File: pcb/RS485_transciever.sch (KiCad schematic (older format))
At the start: 27 parts, among them J1 RJ45_Shielded, J2 RJ45_Shielded, U103 ADM2687E

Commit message: fixing broken symbols
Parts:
- C111, C112, C113, C114, C115, C116, C117, C118: symbol antena:C_Small -> Device:C_Small
- R105: symbol antena:R_Small -> Device:R_Small
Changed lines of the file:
@@
 	4700 3550 4700 750
 $Comp
-L antena:C_Small C?
+L Device:C_Small C?
 U 1 1 5F862E69
 P 7300 2900
@@
 $EndComp
 $Comp
-L antena:C_Small C?
+L Device:C_Small C?
 U 1 1 5F862E6F
 P 7600 2900
@@
 $EndComp
 $Comp
-L antena:C_Small C?
+L Device:C_Small C?
 U 1 1 5F862E75
 P 7300 3200
@@
 $EndComp
 $Comp
-L antena:C_Small C?
+L Device:C_Small C?
 U 1 1 5F862E7B
 P 7600 3200
@@
 $EndComp
 $Comp
-L antena:C_Small C?
+L Device:C_Small C?
 U 1 1 5F862E81
 P 5150 2900
@@
 $EndComp
 $Comp
-L antena:C_Small C?
+L Device:C_Small C?
 U 1 1 5F862E87
 P 4850 2900
@@
 $EndComp
 $Comp
-L antena:C_Small C?
+L Device:C_Small C?
 U 1 1 5F862E8D
 P 5150 3200
@@
 $EndComp
 $Comp
-L antena:C_Small C?
+L Device:C_Small C?
 U 1 1 5F862E93
 P 4850 3200
@@
 Link Tx to Rx (Optional)
 $Comp
-L antena:R_Small R?
+L Device:R_Small R?
 U 1 1 5F862F44
 P 10150 5700

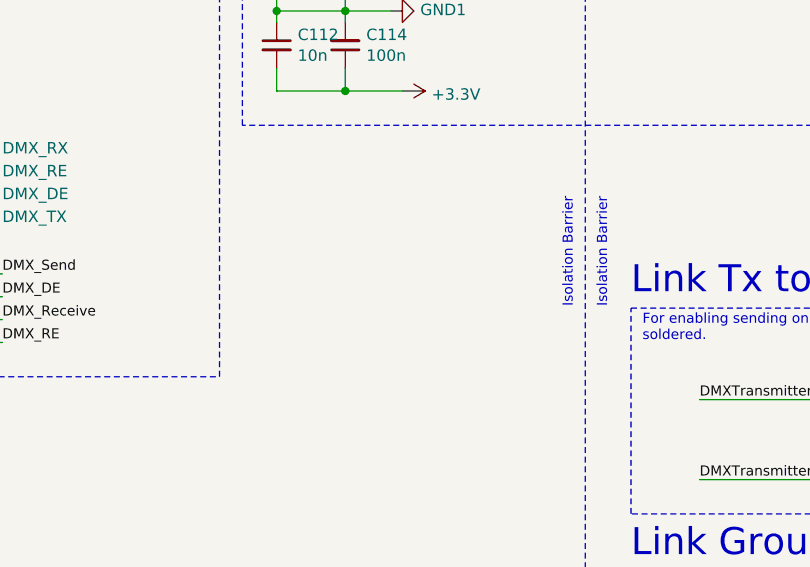
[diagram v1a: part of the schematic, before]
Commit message: Adding protection diodes
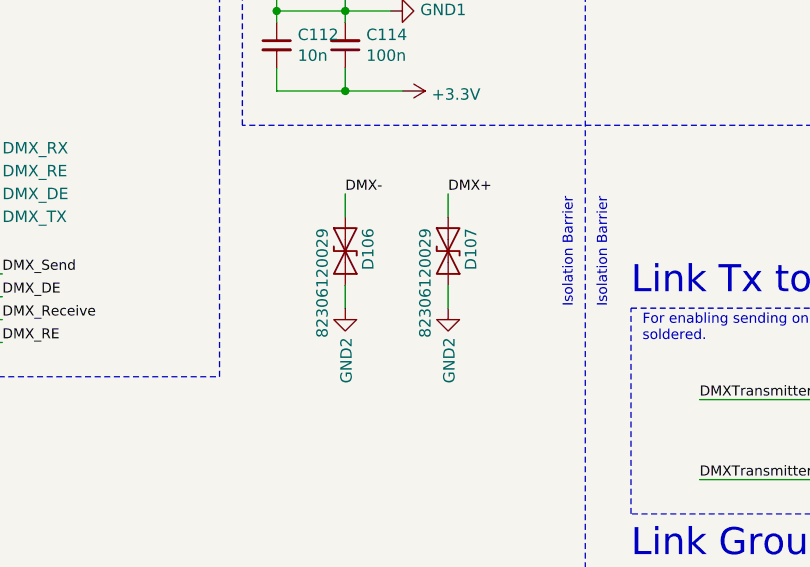
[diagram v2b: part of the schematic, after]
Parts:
- added D106, D107: 82306120029, Diode_SMD:D_0603_1608Metric, symbol Diode:ESD9B3.3ST5G
- JP105, JP106: footprint Jumper:SolderJumper-2_P1.3mm_Open_RoundedPad1.0x1.5mm -> Jumper:SolderJumper-2_P1.3mm_Bridged_RoundedPad1.0x1.5mm
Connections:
- wire segments 93 -> 97
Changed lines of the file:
@@
 F 0 "JP105" H 7650 4955 50  0000 C CNN
 F 1 "SolderJumper_2_Open" H 7650 4864 50  0000 C CNN
-F 2 "Jumper:SolderJumper-2_P1.3mm_Open_RoundedPad1.0x1.5mm" H 7650 4750 50  0001 C CNN
+F 2 "Jumper:SolderJumper-2_P1.3mm_Bridged_RoundedPad1.0x1.5mm" H 7650 4750 50  0001 C CNN
 F 3 "~" H 7650 4750 50  0001 C CNN
 	1    7650 4750
@@
 F 0 "JP106" H 7650 5305 50  0000 C CNN
 F 1 "SolderJumper_2_Open" H 7650 5214 50  0000 C CNN
-F 2 "Jumper:SolderJumper-2_P1.3mm_Open_RoundedPad1.0x1.5mm" H 7650 5100 50  0001 C CNN
+F 2 "Jumper:SolderJumper-2_P1.3mm_Bridged_RoundedPad1.0x1.5mm" H 7650 5100 50  0001 C CNN
 F 3 "~" H 7650 5100 50  0001 C CNN
 	1    7650 5100
@@
 Wire Wire Line
 	9600 1850 9600 1950
+Text Label 5150 3850 0    44   ~ 0
+DMX-
+Text Label 5600 3850 0    44   ~ 0
+DMX+
+$Comp
+L power:GND2 #PWR?
+U 1 1 6081C4D7
+P 5150 4350
+AR Path="/6081C4D7" Ref="#PWR?"  Part="1"
+AR Path="/5F845145/6081C4D7" Ref="#PWR07"  Part="1"
+F 0 "#PWR07" H 5150 4100 50  0001 C CNN
+F 1 "GND2" V 5155 4222 50  0000 R CNN
+F 2 "" H 5150 4350 50  0001 C CNN
+F 3 "" H 5150 4350 50  0001 C CNN
+	1    5150 4350
+	1    0    0    -1
+$EndComp
+$Comp
+L power:GND2 #PWR?
+U 1 1 6081CCE9
+P 5600 4350
+AR Path="/6081CCE9" Ref="#PWR?"  Part="1"
+AR Path="/5F845145/6081CCE9" Ref="#PWR08"  Part="1"
+F 0 "#PWR08" H 5600 4100 50  0001 C CNN
+F 1 "GND2" V 5605 4222 50  0000 R CNN
+F 2 "" H 5600 4350 50  0001 C CNN
+F 3 "" H 5600 4350 50  0001 C CNN
+	1    5600 4350
+	1    0    0    -1
+$EndComp
+Wire Wire Line
+	5150 3850 5150 3950
+Wire Wire Line
+	5600 3850 5600 3950
+Wire Wire Line
+	5150 4250 5150 4350
+Wire Wire Line
+	5600 4250 5600 4350
+$Comp
+L Diode:ESD9B3.3ST5G D?
+U 1 1 608502C5
+P 5150 4100
+AR Path="/608502C5" Ref="D?"  Part="1"
+AR Path="/5F845145/608502C5" Ref="D106"  Part="1"
+F 0 "D106" H 5050 4200 50  0000 L CNN
+F 1 "82306120029" H 5050 4000 50  0000 L CNN
+F 2 "Diode_SMD:D_0603_1608Metric" H 5150 4100 50  0001 C CNN
+F 3 "https://hr.mouser.com/datasheet/2/445/82306120029-1724892.pdf" H 5150 4100 50  0001 C CNN
+F 4 "https://hr.mouser.com/ProductDetail/Wurth-Elektronik/82306120029?qs=2kOmHSv6VfRx19zH7vCkmQ%3D%3D" V 5150 4100 50  0001 C CNN "Mouser"
+	1    5150 4100
+	0    1    1    0
+$EndComp
+$Comp
+L Diode:ESD9B3.3ST5G D?
+U 1 1 6085384B
+P 5600 4100
+AR Path="/6085384B" Ref="D?"  Part="1"
+AR Path="/5F845145/6085384B" Ref="D107"  Part="1"
+F 0 "D107" H 5500 4200 50  0000 L CNN
+F 1 "82306120029" H 5500 4000 50  0000 L CNN
+F 2 "Diode_SMD:D_0603_1608Metric" H 5600 4100 50  0001 C CNN
+F 3 "https://hr.mouser.com/datasheet/2/445/82306120029-1724892.pdf" H 5600 4100 50  0001 C CNN
+F 4 "https://hr.mouser.com/ProductDetail/Wurth-Elektronik/82306120029?qs=2kOmHSv6VfRx19zH7vCkmQ%3D%3D" V 5600 4100 50  0001 C CNN "Mouser"
+	1    5600 4100
+	0    1    1    0
+$EndComp
 $EndSCHEMATC
